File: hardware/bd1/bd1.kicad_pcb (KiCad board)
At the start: 2 copper layers, 138.2 x 104.9 mm, 90 parts, among them J1 Conn_02x03_Odd_Even, J2 USB_C_Receptacle_USB2.0, J20 USB_C_Receptacle_USB2.0, J3 SJ-43514, J30 SJ-43514, U1 STM32L412CBTx, U2 AP2127N-3.3

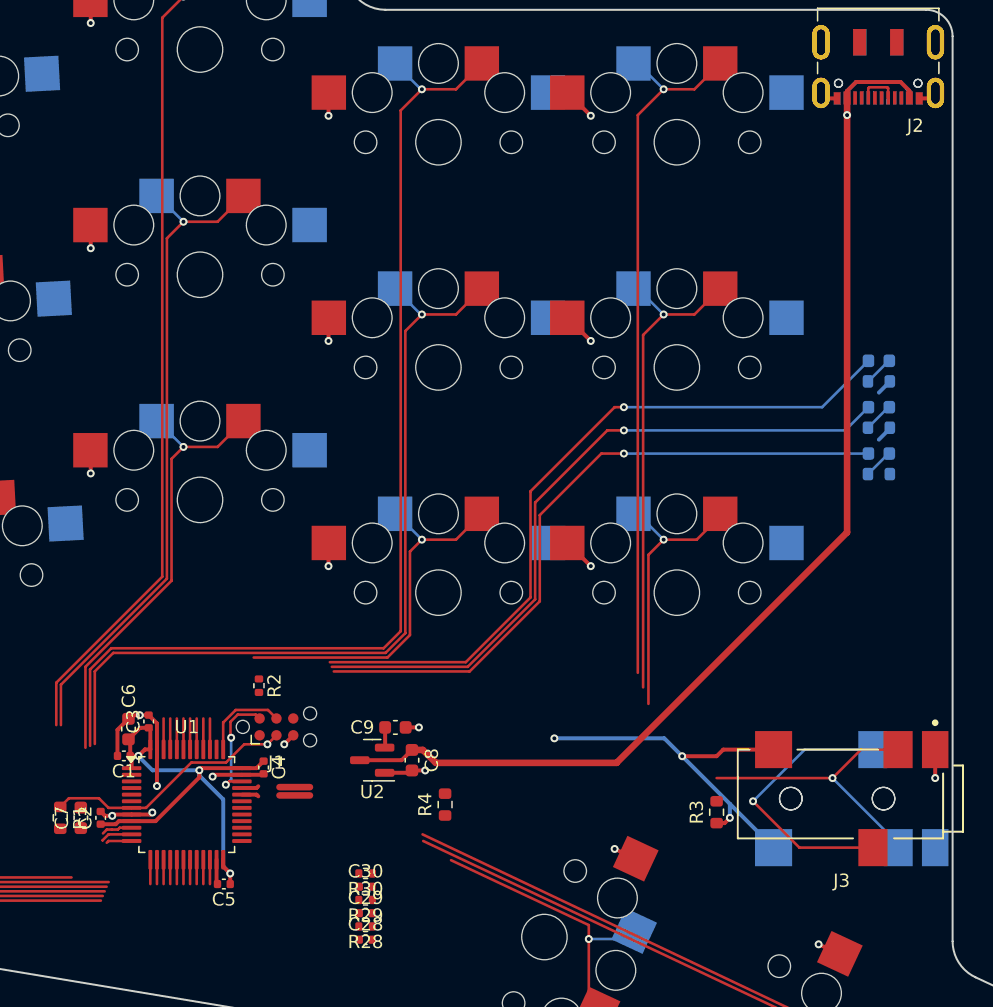
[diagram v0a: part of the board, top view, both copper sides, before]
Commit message: USB routing
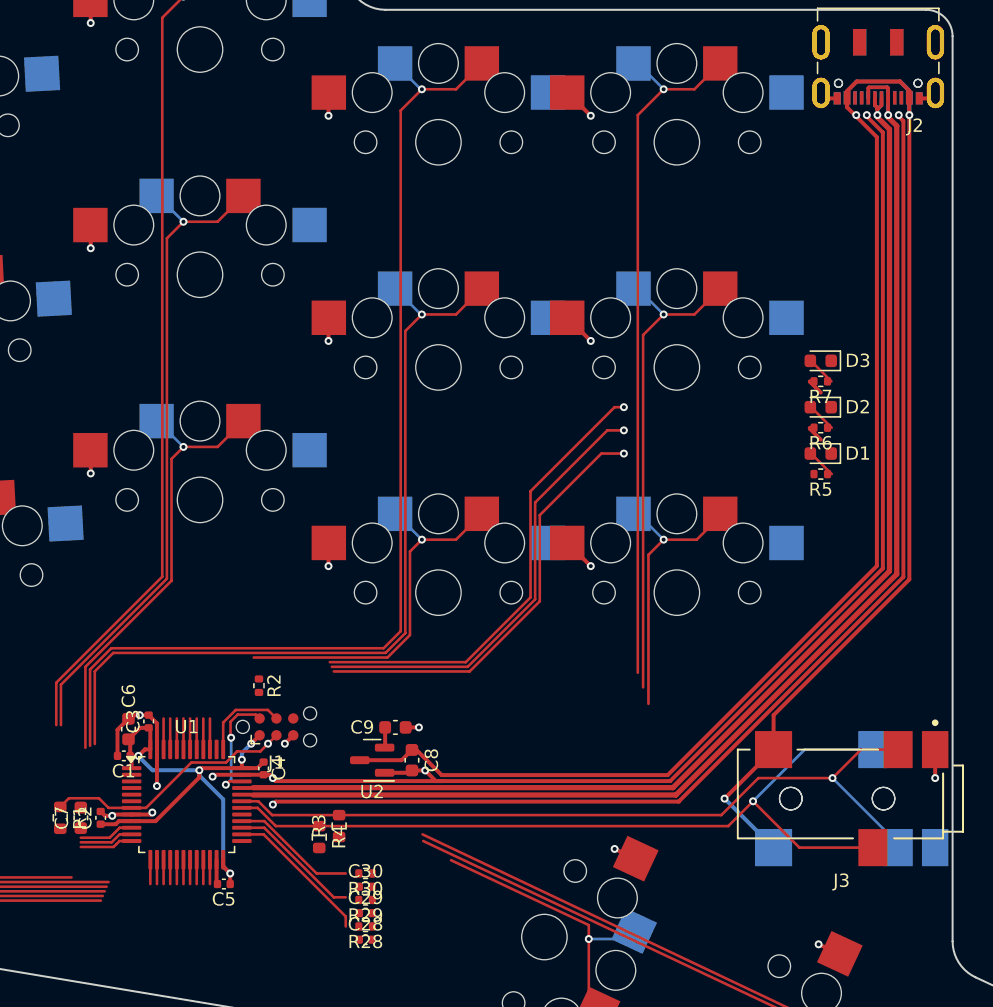
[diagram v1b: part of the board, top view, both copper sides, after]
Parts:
- C10, C11, C12, C13, C14, C15, C16, C17, C18, C19, C20, C21, C22, C23, C24, C25, C26, C27, C28, C29, C30: value 0.1uF -> 4700p
- D1, D2, D3: moved to F.Cu
- R10, R11, R12, R13, R14, R15, R16, R17, R18, R19, R20, R21, R22, R23, R24, R25, R26, R27, R28, R29, R30: value 1k -> 470
- R5, R6, R7: footprint Resistor_SMD:R_0603_1608Metric -> Resistor_SMD:R_0402_1005Metric; moved to F.Cu
- moved R3 28.5 mm to (232.5, 167.6)
- moved R4 9.81 mm to (231.0, 168.4), turned to 90 degrees
- moved D1 4.39 mm to (268.9, 139.5), turned to 180 degrees
- moved D2 4.39 mm to (268.9, 136.0), turned to 180 degrees
- moved D3 4.39 mm to (268.9, 132.5), turned to 180 degrees
- moved R5 4.39 mm to (268.9, 141.1), turned to 180 degrees
- moved R6 4.39 mm to (268.9, 137.6), turned to 180 degrees
- moved R7 4.39 mm to (268.9, 134.1), turned to 180 degrees
- moved C4 0.07 mm to (226.8, 163.3)
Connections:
- J2 pad A6: /Connectors/USB_DP -> /USB_DP
- J2 pad A7: /Connectors/USB_DN -> /USB_DN
- J2 pad B6: /Connectors/USB_DP -> /USB_DP
- J2 pad B7: /Connectors/USB_DN -> /USB_DN
- J20 pad A6: /Connectors/USB_DP -> /USB_DP
- J20 pad A7: /Connectors/USB_DN -> /USB_DN
- J20 pad B6: /Connectors/USB_DP -> /USB_DP
- J20 pad B7: /Connectors/USB_DN -> /USB_DN
- J3 pad 3: /SDA -> /SCL
- J3 pad 4: /SCL -> /SDA
- J30 pad 3: /SDA -> /SCL
- J30 pad 4: /SCL -> /SDA
- U1 pad 39: unconnected-(U1-PB3-Pad39) -> /LED0
- U1 pad 40: unconnected-(U1-PB4-Pad40) -> /LED1
- U1 pad 41: unconnected-(U1-PB5-Pad41) -> /LED2
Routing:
- net GND: track 75.4 -> 255.2 mm, vias 30 -> 34
- net /USB_DN: track 3.59 -> 99.1 mm, vias 0 -> 1
- net /USB_DP: track 3.59 -> 94.4 mm, vias 0 -> 1
- net +5V: track 91.4 -> 160.3 mm, vias 1 -> 3
- net /SCL: track 21.9 -> 61.1 mm
- net /SDA: track 21.2 -> 59.3 mm
- net +3V3: track 69.0 -> 42.7 mm, vias 6 -> 5
- net /LED2: track 54.8 -> 37.2 mm
- net /LED1: track 52.9 -> 36.1 mm
- net /LED0: track 51.0 -> 34.9 mm
- net unconnected-(U1-PB13-Pad26): track 0.00 -> 11.2 mm
- net unconnected-(U1-PB14-Pad27): track 0.00 -> 10.0 mm
- net unconnected-(U1-PB15-Pad28): track 0.00 -> 9.47 mm
- net /Connectors/USB_DN: track 3.02 -> 0.00 mm
- net unconnected-(U1-PB5-Pad41): track 2.34 -> 0.00 mm
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
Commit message: Solved routing
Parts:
- C1, C2, C3, C4, C5: footprint Capacitor_SMD:C_0402_1005Metric -> Capacitor_SMD:C_0603_1608Metric
- C10, C11, C12, C13, C14, C15, C16, C17, C18, C19, C20, C21, C22, C23, C24, C25, C26, C27, C28, C29, C30: footprint Capacitor_SMD:C_0402_1005Metric -> Capacitor_SMD:C_0603_1608Metric; moved to B.Cu
- R10, R11, R12, R13, R14, R15, R16, R17, R18, R19, R2, R20, R21, R22, R23, R24, R25, R26, R27, R28, R29, R30, R5, R6, R7: footprint Resistor_SMD:R_0402_1005Metric -> Resistor_SMD:R_0603_1608Metric
- moved C24 122.0 mm to (212.9, 169.9)
- moved C19 118.5 mm to (212.9, 171.3), turned to 180 degrees
- moved C20 117.8 mm to (213.8, 173.6), turned to -90 degrees
- moved C17 115.9 mm to (217.9, 173.6), turned to -90 degrees
- moved C21 115.8 mm to (215.2, 173.6), turned to -90 degrees
- moved C23 115.6 mm to (212.9, 168.6)
- moved C18 113.9 mm to (219.3, 173.6), turned to -90 degrees
- moved C27 110.8 mm to (219.6, 157.7), turned to 90 degrees
- moved C16 110.6 mm to (216.6, 173.6), turned to -90 degrees
- moved C26 109.9 mm to (220.9, 157.7), turned to 90 degrees
- moved C25 108.9 mm to (222.3, 157.7), turned to 90 degrees
- moved C22 108.7 mm to (218.2, 157.7), turned to 90 degrees
- moved C13 108.5 mm to (220.8, 173.6), turned to -90 degrees
- moved R24 107.5 mm to (212.9, 169.9)
- moved C10 106.8 mm to (224.9, 173.6), turned to -90 degrees
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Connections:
- C10 pad 1: Net-(C10-Pad1) -> /PB10
- C11 pad 1: Net-(C11-Pad1) -> /PB11
- C12 pad 1: Net-(C12-Pad1) -> /PB12
- C13 pad 1: Net-(C13-Pad1) -> /PB00
- C14 pad 1: Net-(C14-Pad1) -> /PB01
- C15 pad 1: Net-(C15-Pad1) -> /PB02
- C16 pad 1: Net-(C16-Pad1) -> /PA05
- C17 pad 1: Net-(C17-Pad1) -> /PA06
- C18 pad 1: Net-(C18-Pad1) -> /PA07
- C19 pad 1: Net-(C19-Pad1) -> /PA02
- C20 pad 1: Net-(C20-Pad1) -> /PA03
- C21 pad 1: Net-(C21-Pad1) -> /PA04
- C22 pad 1: Net-(C22-Pad1) -> /PB09
- C23 pad 1: Net-(C23-Pad1) -> /PA00
- C24 pad 1: Net-(C24-Pad1) -> /PA01
- C25 pad 1: Net-(C25-Pad1) -> /PB06
- C26 pad 1: Net-(C26-Pad1) -> /PB07
- C27 pad 1: Net-(C27-Pad1) -> /PB08
- C28 pad 1: Net-(C28-Pad1) -> /PB13
- C29 pad 1: Net-(C29-Pad1) -> /PB14
- C30 pad 1: Net-(C30-Pad1) -> /PB15
- R10 pad 2: Net-(C10-Pad1) -> /PB10
- R11 pad 2: Net-(C11-Pad1) -> /PB11
- R12 pad 2: Net-(C12-Pad1) -> /PB12
- R13 pad 2: Net-(C13-Pad1) -> /PB00
- R14 pad 2: Net-(C14-Pad1) -> /PB01
- R15 pad 2: Net-(C15-Pad1) -> /PB02
- R16 pad 2: Net-(C16-Pad1) -> /PA05
- R17 pad 2: Net-(C17-Pad1) -> /PA06
- R18 pad 2: Net-(C18-Pad1) -> /PA07
- R19 pad 2: Net-(C19-Pad1) -> /PA02
- R20 pad 2: Net-(C20-Pad1) -> /PA03
- R21 pad 2: Net-(C21-Pad1) -> /PA04
- R22 pad 2: Net-(C22-Pad1) -> /PB09
- R23 pad 2: Net-(C23-Pad1) -> /PA00
- R24 pad 2: Net-(C24-Pad1) -> /PA01
- R25 pad 2: Net-(C25-Pad1) -> /PB06
- R26 pad 2: Net-(C26-Pad1) -> /PB07
- R27 pad 2: Net-(C27-Pad1) -> /PB08
- R28 pad 2: Net-(C28-Pad1) -> /PB13
- R29 pad 2: Net-(C29-Pad1) -> /PB14
- R30 pad 2: Net-(C30-Pad1) -> /PB15
- U1 pad 10: unconnected-(U1-PA0-Pad10) -> /PA00
- U1 pad 11: unconnected-(U1-PA1-Pad11) -> /PA01
- U1 pad 12: unconnected-(U1-PA2-Pad12) -> /PA02
- U1 pad 13: unconnected-(U1-PA3-Pad13) -> /PA03
- U1 pad 14: unconnected-(U1-PA4-Pad14) -> /PA04
- U1 pad 15: unconnected-(U1-PA5-Pad15) -> /PA05
- U1 pad 16: unconnected-(U1-PA6-Pad16) -> /PA06
- U1 pad 17: unconnected-(U1-PA7-Pad17) -> /PA07
- U1 pad 18: unconnected-(U1-PB0-Pad18) -> /PB00
- U1 pad 19: unconnected-(U1-PB1-Pad19) -> /PB01
- U1 pad 20: unconnected-(U1-PB2-Pad20) -> /PB02
- U1 pad 21: unconnected-(U1-PB10-Pad21) -> /PB10
- U1 pad 22: unconnected-(U1-PB11-Pad22) -> /PB11
- U1 pad 25: unconnected-(U1-PB12-Pad25) -> /PB12
- U1 pad 26: unconnected-(U1-PB13-Pad26) -> /PB13
- U1 pad 27: unconnected-(U1-PB14-Pad27) -> /PB14
- U1 pad 28: unconnected-(U1-PB15-Pad28) -> /PB15
- U1 pad 39: /LED0 -> /LED2
- U1 pad 41: /LED2 -> /LED0
- U1 pad 42: unconnected-(U1-PB6-Pad42) -> /PB06
- U1 pad 43: unconnected-(U1-PB7-Pad43) -> /PB07
- U1 pad 45: unconnected-(U1-PB8-Pad45) -> /PB08
- U1 pad 46: unconnected-(U1-PB9-Pad46) -> /PB09
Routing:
- net /LED2: track 37.2 -> 69.6 mm, vias 1 -> 0
- net /inner_top: track 53.0 -> 85.4 mm
- net /inner_home: track 37.0 -> 67.2 mm
- net /LED1: track 36.1 -> 66.0 mm, vias 1 -> 0
- net +3V3: track 42.7 -> 72.0 mm, vias 5 -> 7
- net /inner_bottom: track 21.1 -> 49.2 mm
- net /LED0: track 34.9 -> 62.4 mm, vias 1 -> 0
- net /ring_top: track 64.6 -> 85.9 mm
- net /ring_home: track 46.8 -> 66.7 mm
- net /middle_top: track 67.1 -> 86.3 mm
- net /ring_bottom: track 29.0 -> 47.3 mm
- net /outer_top: track 98.6 -> 115.4 mm
- net /middle_home: track 50.0 -> 66.4 mm
- net /outer_home: track 80.8 -> 96.0 mm
- net /outer_bottom: track 63.3 -> 76.8 mm
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
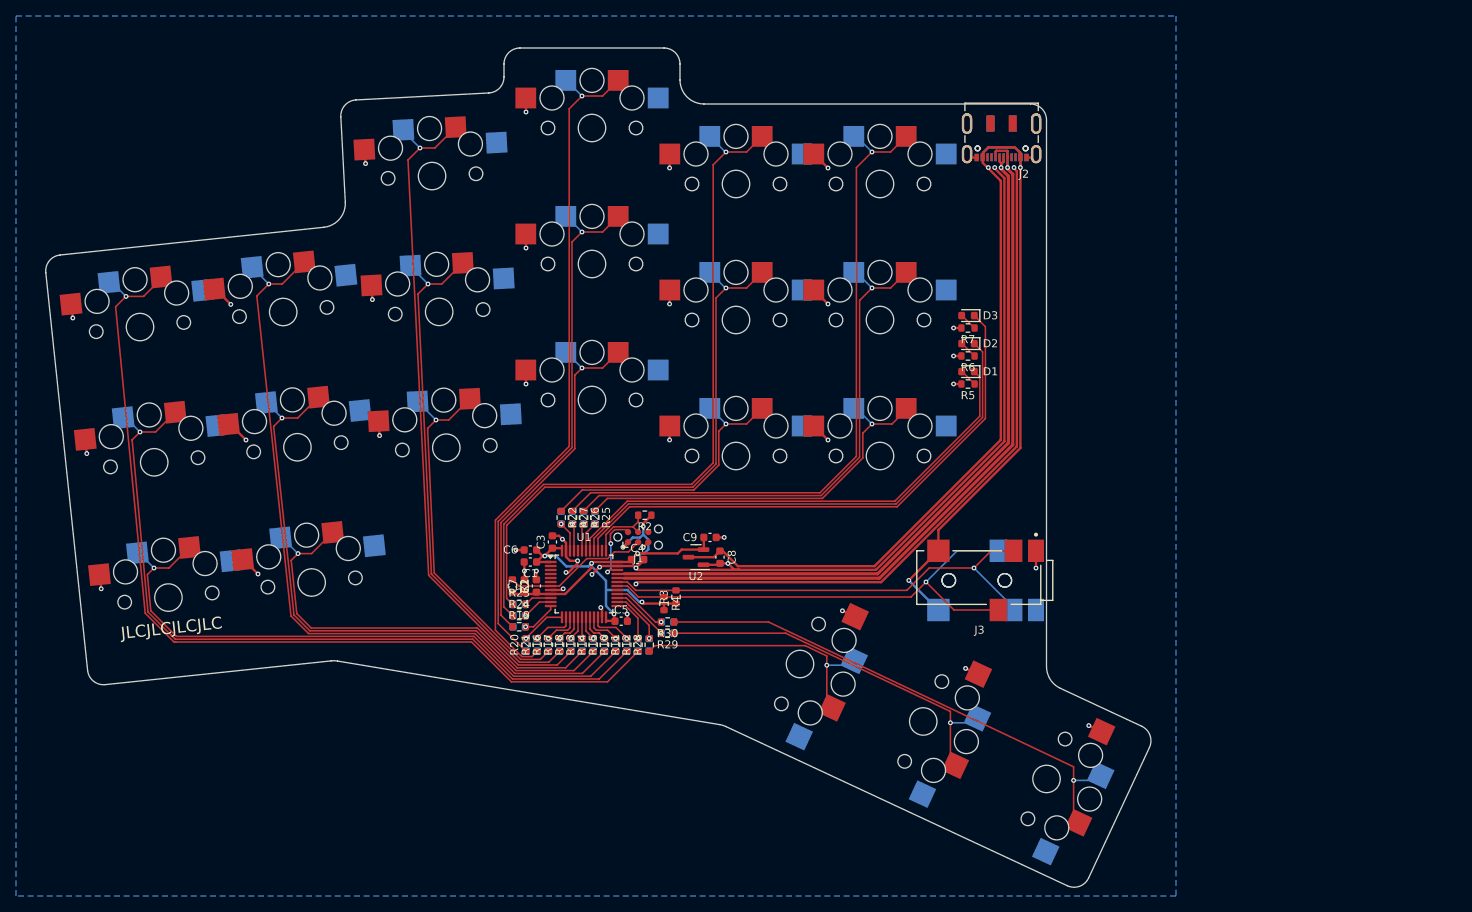
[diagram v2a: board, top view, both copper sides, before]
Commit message: Shift MCU so programmer has room
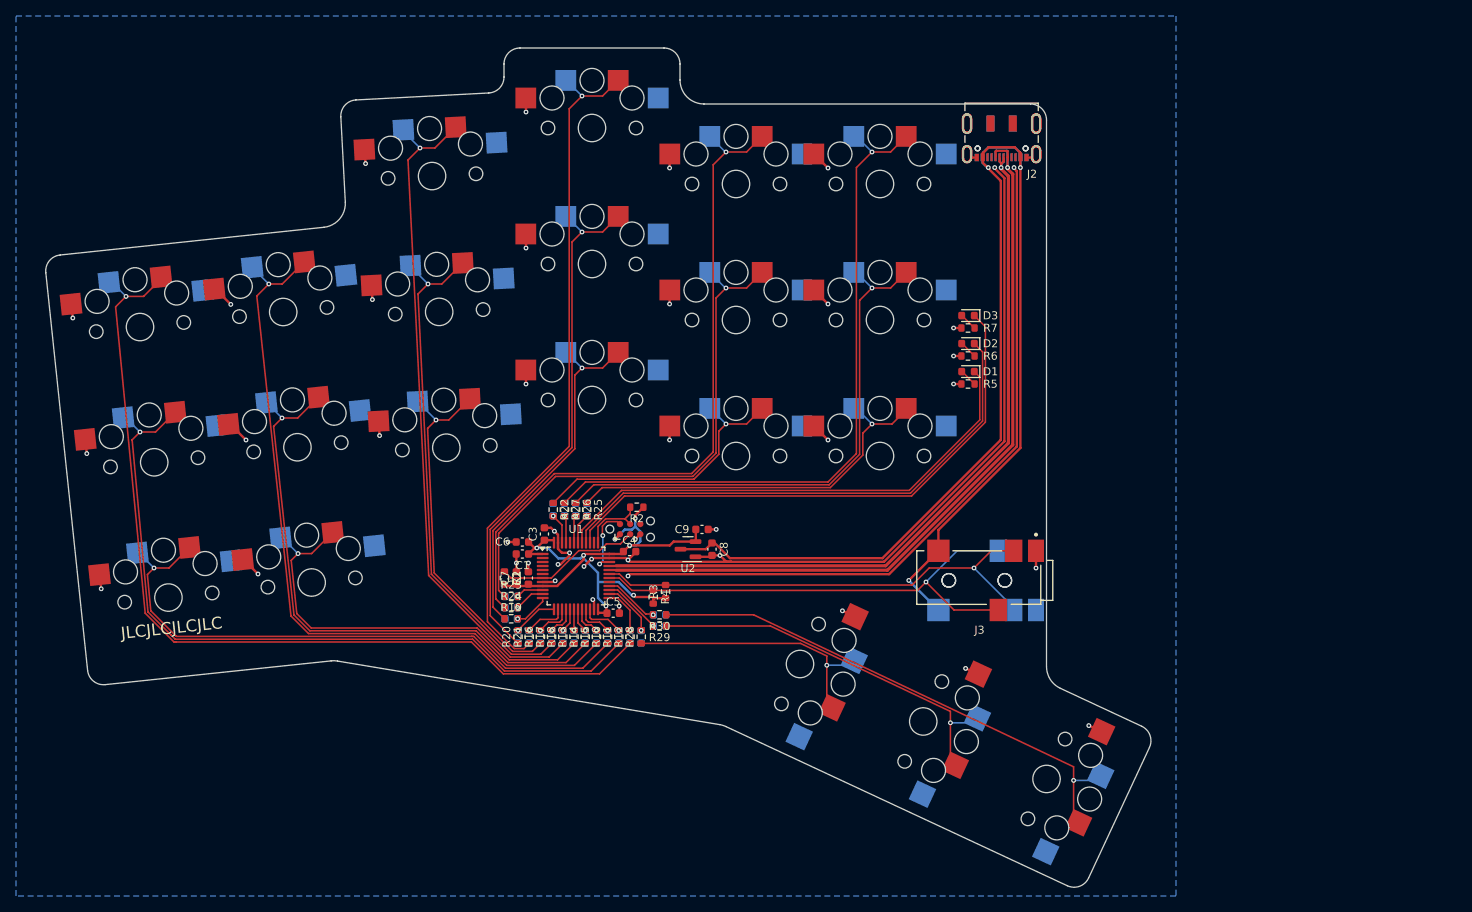
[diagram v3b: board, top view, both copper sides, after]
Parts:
- moved G*** 8.04 mm to (273.0, 133.0)
- moved R4 1.58 mm to (229.7, 167.6)
- moved R3 1.46 mm to (231.2, 166.9)
- moved C1 1.41 mm to (213.3, 162.2)
- moved C10 1.41 mm to (223.9, 172.6)
- moved C11 1.41 mm to (225.3, 172.6)
- moved C12 1.41 mm to (226.8, 172.6)
- moved C13 1.41 mm to (219.8, 172.6)
- moved C14 1.41 mm to (221.2, 172.6)
- moved C15 1.41 mm to (222.6, 172.6)
- moved C16 1.41 mm to (215.6, 172.6)
- moved C17 1.41 mm to (216.9, 172.6)
- moved C18 1.41 mm to (218.3, 172.6)
- moved C19 1.41 mm to (211.9, 170.3)
- moved C2 1.41 mm to (214.1, 165.2)
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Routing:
- net +5V: track 160.3 -> 162.5 mm
- net /ring_home: track 66.7 -> 65.2 mm
- net /pinky_top: track 94.2 -> 92.7 mm
- net /ring_bottom: track 47.3 -> 45.9 mm
- net /pinky_home: track 74.9 -> 73.4 mm
- net /outer_home: track 96.0 -> 94.6 mm
- net /outer_top: track 115.4 -> 114.0 mm
- net /outer_bottom: track 76.8 -> 75.4 mm
- net /pinky_bottom: track 55.6 -> 54.2 mm
- net /ring_top: track 85.9 -> 84.5 mm
- net /index_top: track 88.9 -> 87.5 mm
- net /index_home: track 70.2 -> 68.8 mm
- net /far_thumb: track 64.9 -> 66.1 mm
- net /home_thumb: track 47.4 -> 48.6 mm
- net GND: track 258.0 -> 259.2 mm
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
